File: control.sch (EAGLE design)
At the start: 103 parts, among them CN1 40PIN FPC, CN2 MINI B USB, CN3 2X10 HEADER, CN4 2X10 HEADER, SW1 TACT, SW10 TACT, SW11 TACT, SW12 TACT, SW13 TACT, SW14 TACT, SW15 TACT, SW16 TACT, SW2 TACT, SW3 TACT, SW4 TACT, SW5 TACT, SW6 TACT, SW7 TACT, SW8 TACT, SW9 TACT, U1 STM32H743ZI, U2 AS4C8M16SA, U3 TPS61169, U4 USBLC6-2SC6, U5 FT230X, U6 DCDC 3V3

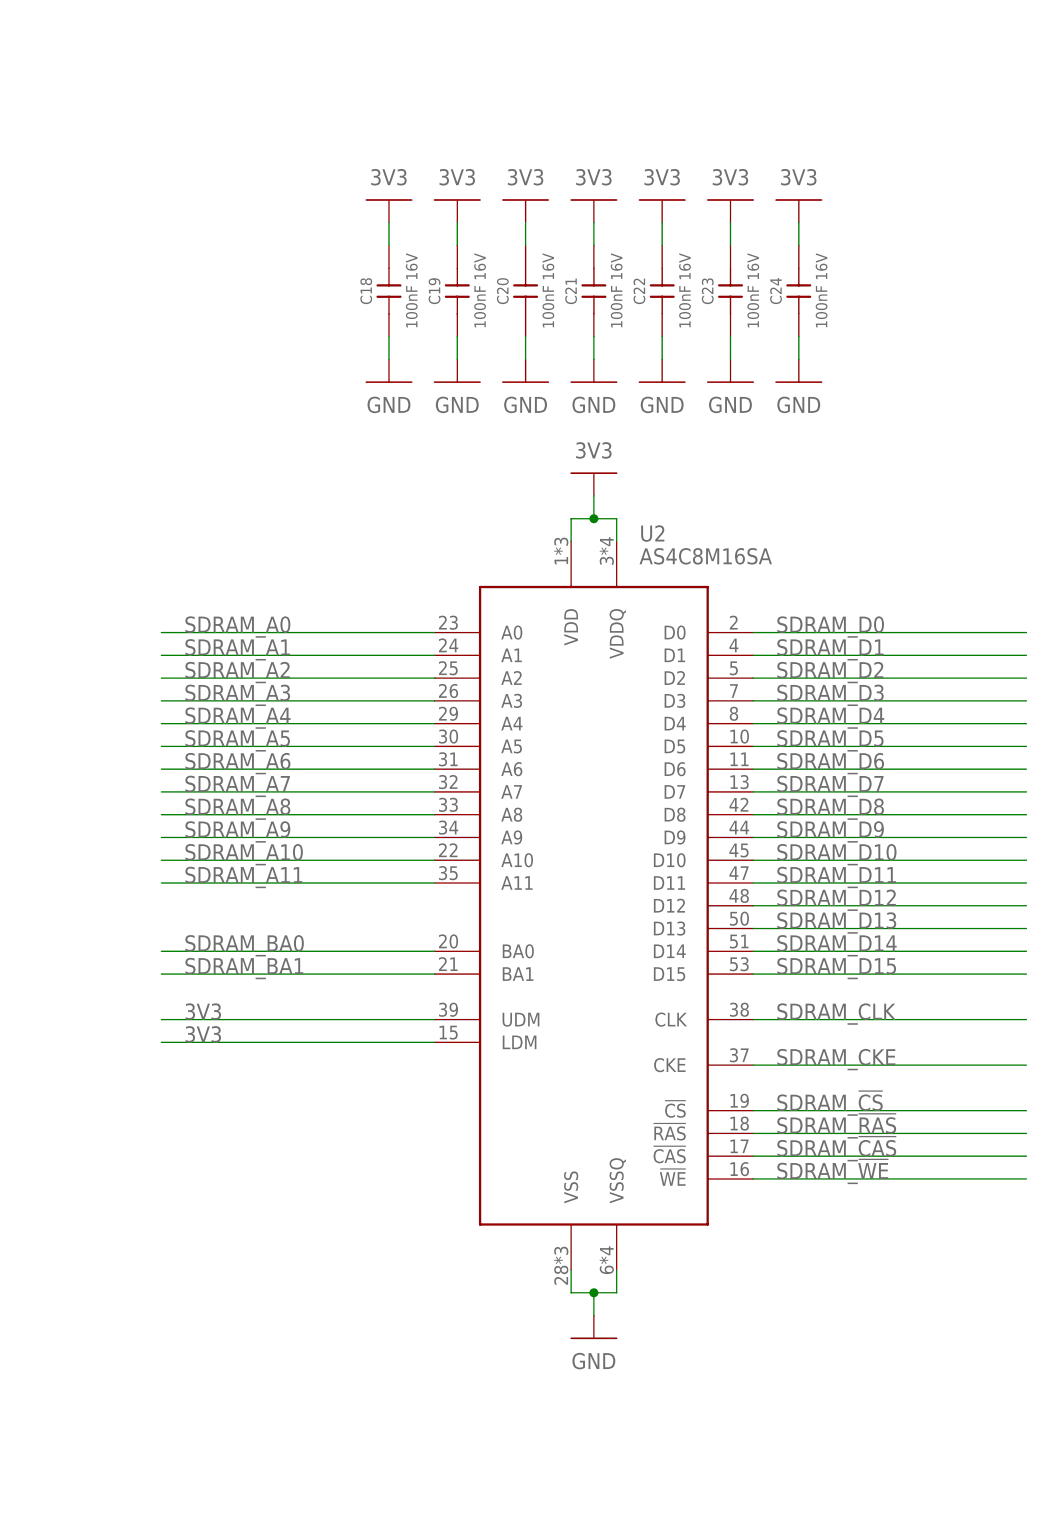
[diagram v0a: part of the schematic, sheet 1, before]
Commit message: Fixes for stability
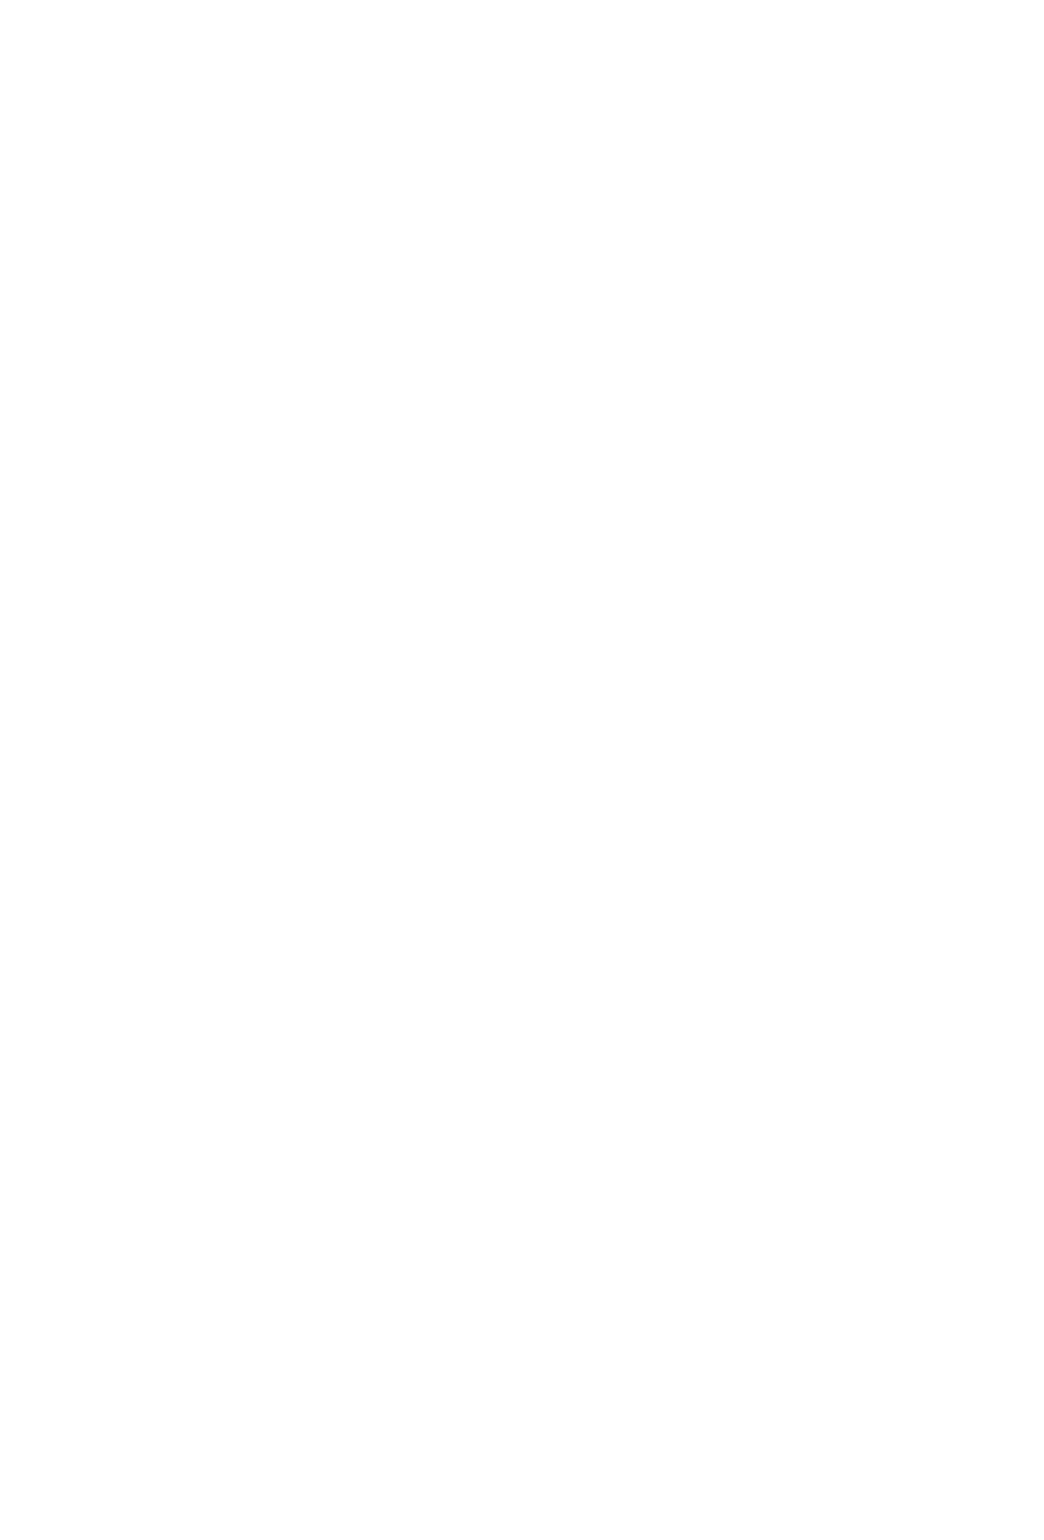
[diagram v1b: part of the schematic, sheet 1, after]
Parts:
- removed C18, C19, C20, C21, C22, C23, C24: 100nF 16V, CAPACITORS:CL10B104KO8WPNC
- removed U2: AS4C8M16SA, ICs:AS4C8M16SA
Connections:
- net 3V3: no longer C18.2, C19.2, C20.2, C21.2, C22.2, C23.2, C24.2, U2.LDM, U2.UDM, U2.VDD, U2.VDDQ
- net GND: no longer C18.1, C19.1, C20.1, C21.1, C22.1, C23.1, C24.1, U2.VSS, U2.VSSQ
- net SDRAM_!CAS: no longer U2.!CAS
- net SDRAM_!CS: no longer U2.!CS
- net SDRAM_!RAS: no longer U2.!RAS
- net SDRAM_!WE: no longer U2.!WE
- net SDRAM_A0: no longer U2.A0
- net SDRAM_A1: no longer U2.A1
- net SDRAM_A10: no longer U2.A10
- net SDRAM_A11: no longer U2.A11
- net SDRAM_A2: no longer U2.A2
- net SDRAM_A3: no longer U2.A3
- net SDRAM_A4: no longer U2.A4
- net SDRAM_A5: no longer U2.A5
- net SDRAM_A6: no longer U2.A6
- net SDRAM_A7: no longer U2.A7
- net SDRAM_A8: no longer U2.A8
- net SDRAM_A9: no longer U2.A9
- net SDRAM_BA0: no longer U2.BA0
- net SDRAM_BA1: no longer U2.BA1
- net SDRAM_CKE: no longer U2.CKE
- net SDRAM_CLK: no longer U2.CLK
- net SDRAM_D0: no longer U2.D0
- net SDRAM_D1: no longer U2.D1
- net SDRAM_D10: no longer U2.D10
- net SDRAM_D11: no longer U2.D11
- net SDRAM_D12: no longer U2.D12
- net SDRAM_D13: no longer U2.D13
- net SDRAM_D14: no longer U2.D14
- net SDRAM_D15: no longer U2.D15
- net SDRAM_D2: no longer U2.D2
- net SDRAM_D3: no longer U2.D3
- net SDRAM_D4: no longer U2.D4
- net SDRAM_D5: no longer U2.D5
- net SDRAM_D6: no longer U2.D6
- net SDRAM_D7: no longer U2.D7
- net SDRAM_D8: no longer U2.D8
- net SDRAM_D9: no longer U2.D9
